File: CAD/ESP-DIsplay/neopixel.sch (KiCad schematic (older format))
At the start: 3 parts, among them J701 Neo

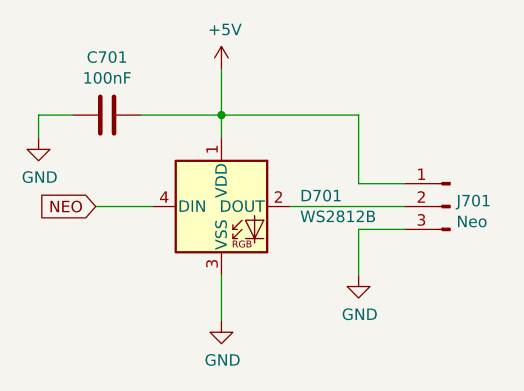
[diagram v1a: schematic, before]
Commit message: ESP Display v1
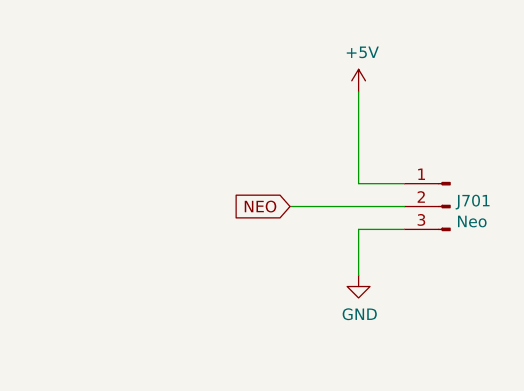
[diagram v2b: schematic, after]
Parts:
- removed C701: 100nF, Capacitor_SMD:C_1206_3216Metric, symbol Device:C
- removed D701: WS2812B, LED_SMD:LED_WS2812B_PLCC4_5.0x5.0mm_P3.2mm, symbol LED:WS2812B
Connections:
- net NEO: now also J701.2 (Pin_2)
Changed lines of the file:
@@
 $Descr A4 11693 8268
 encoding utf-8
-Sheet 8 9
+Sheet 7 8
 Title ""
 Date ""
@@
 Comment4 ""
 $EndDescr
-Wire Wire Line
-	4600 3600 4850 3600
-Text GLabel 4600 3600 0    50   Input ~ 0
+Text GLabel 5450 3600 0    50   Input ~ 0
 NEO
-Wire Wire Line
-	5150 3900 5150 4100
-$Comp
-L power:GND #PWR?
-U 1 1 603C6ED7
-P 5150 4100
-AR Path="/603C6ED7" Ref="#PWR?"  Part="1"
-AR Path="/60C58A4D/603BB4B3/603C6ED7" Ref="#PWR0703"  Part="1"
-F 0 "#PWR0703" H 5150 3850 50  0001 C CNN
-F 1 "GND" H 5155 3927 50  0000 C CNN
-F 2 "" H 5150 4100 50  0001 C CNN
-F 3 "" H 5150 4100 50  0001 C CNN
-	1    5150 4100
-	1    0    0    -1
-$EndComp
-$Comp
-L LED:WS2812B D?
-U 1 1 603C6EDD
-P 5150 3600
-AR Path="/603C6EDD" Ref="D?"  Part="1"
-AR Path="/60C58A4D/603BB4B3/603C6EDD" Ref="D701"  Part="1"
-F 0 "D701" H 5494 3646 50  0000 L CNN
-F 1 "WS2812B" H 5494 3555 50  0000 L CNN
-F 2 "LED_SMD:LED_WS2812B_PLCC4_5.0x5.0mm_P3.2mm" H 5200 3300 50  0001 L TNN
-F 3 "https://cdn-shop.adafruit.com/datasheets/WS2812B.pdf" H 5250 3225 50  0001 L TNN
-	1    5150 3600
-	1    0    0    -1
-$EndComp
 $Comp
 L power:+5V #PWR?
 U 1 1 603C6EE3
-P 5150 3000
+P 5750 3100
 AR Path="/603C6EE3" Ref="#PWR?"  Part="1"
 AR Path="/60C58A4D/603BB4B3/603C6EE3" Ref="#PWR0702"  Part="1"
-F 0 "#PWR0702" H 5150 2850 50  0001 C CNN
-F 1 "+5V" H 5165 3173 50  0000 C CNN
-F 2 "" H 5150 3000 50  0001 C CNN
-F 3 "" H 5150 3000 50  0001 C CNN
-	1    5150 3000
+F 0 "#PWR0702" H 5750 2950 50  0001 C CNN
+F 1 "+5V" H 5765 3273 50  0000 C CNN
+F 2 "" H 5750 3100 50  0001 C CNN
+F 3 "" H 5750 3100 50  0001 C CNN
+	1    5750 3100
 	1    0    0    -1
 $EndComp
@@
 $EndComp
 Wire Wire Line
-	5150 3000 5150 3200
-Wire Wire Line
-	5150 3200 5750 3200
-Wire Wire Line
-	5750 3200 5750 3500
-Wire Wire Line
 	5750 3500 5950 3500
-Connection ~ 5150 3200
-Wire Wire Line
-	5150 3200 5150 3300
 Wire Wire Line
 	5450 3600 5950 3600
@@
 Wire Wire Line
 	5750 3700 5750 3900
-$Comp
-L Device:C C?
-U 1 1 603C6EFE
-P 4650 3200
-AR Path="/603C6EFE" Ref="C?"  Part="1"
-AR Path="/60C58A4D/603BB4B3/603C6EFE" Ref="C701"  Part="1"
-F 0 "C701" V 4398 3200 50  0000 C CNN
-F 1 "100nF" V 4489 3200 50  0000 C CNN
-F 2 "Capacitor_SMD:C_1206_3216Metric" H 4688 3050 50  0001 C CNN
-F 3 "~" H 4650 3200 50  0001 C CNN
-	1    4650 3200
-	0    1    1    0
-$EndComp
-$Comp
-L power:GND #PWR?
-U 1 1 603C6F04
-P 4350 3300
-AR Path="/603C6F04" Ref="#PWR?"  Part="1"
-AR Path="/60C58A4D/603BB4B3/603C6F04" Ref="#PWR0701"  Part="1"
-F 0 "#PWR0701" H 4350 3050 50  0001 C CNN
-F 1 "GND" H 4355 3127 50  0000 C CNN
-F 2 "" H 4350 3300 50  0001 C CNN
-F 3 "" H 4350 3300 50  0001 C CNN
-	1    4350 3300
-	1    0    0    -1
-$EndComp
 Wire Wire Line
-	4500 3200 4350 3200
-Wire Wire Line
-	4800 3200 5150 3200
-Wire Wire Line
-	4350 3200 4350 3300
+	5750 3100 5750 3500
 $EndSCHEMATC
